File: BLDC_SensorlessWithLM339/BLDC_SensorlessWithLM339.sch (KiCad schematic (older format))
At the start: 48 parts, among them J1 Conn_01x04_Female, J2 Conn_01x07_Female, J3 Screw_Terminal_01x02, J4 Screw_Terminal_01x03, Q1 50N06, Q2 50N06, Q3 50N06, Q4 50N06, Q5 50N06, Q6 50N06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

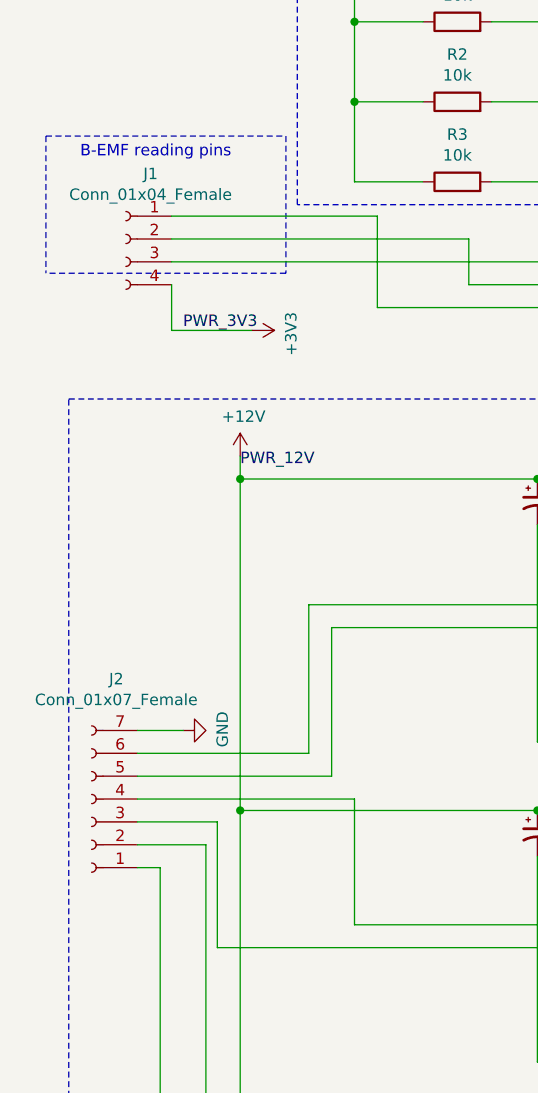
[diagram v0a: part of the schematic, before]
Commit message: Updated to Version 0.2
Updated to version 0.2. Now pcb holds only 10x10 cm^2 field.
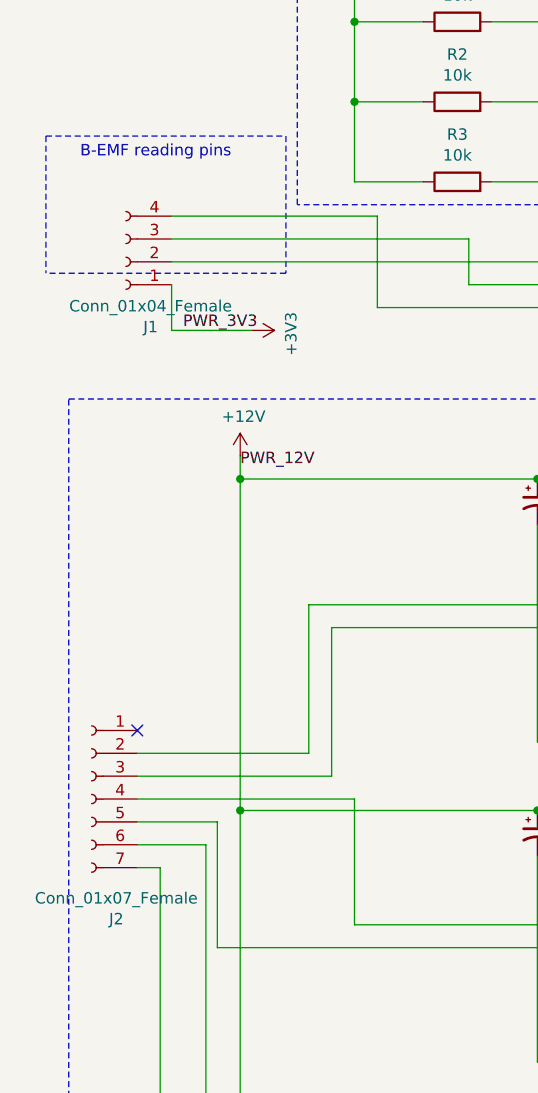
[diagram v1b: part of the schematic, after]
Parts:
- J1: footprint Connector_PinSocket_1.27mm:PinSocket_1x04_P1.27mm_Vertical -> Connector_PinSocket_2.54mm:PinSocket_1x04_P2.54mm_Vertical
- J2: footprint Connector_PinSocket_1.27mm:PinSocket_1x07_P1.27mm_Vertical -> Connector_PinSocket_2.54mm:PinSocket_1x07_P2.54mm_Vertical
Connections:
- net +3V3: now also J1.1 (Pin_1); no longer J1.4 (Pin_4)
- net GND: no longer J2.7 (Pin_7)
- net at R2.2, U4.1 (OUT2): now also J1.3 (Pin_3); no longer J1.2 (Pin_2)
- net at R1.2, U4.14 (OUT3): now also J1.2 (Pin_2); no longer J1.3 (Pin_3)
- net at R3.2, U4.2 (OUT1): now also J1.4 (Pin_4); no longer J1.1 (Pin_1)
- net at J2.1 (Pin_1): no longer U3.3 (LIN)
- net at J2.2 (Pin_2): now also U1.2 (HIN); no longer U3.2 (HIN)
- net at J2.3 (Pin_3): now also U1.3 (LIN); no longer U2.3 (LIN)
- net at J2.5 (Pin_5): now also U2.3 (LIN); no longer U1.3 (LIN)
- net at J2.6 (Pin_6): now also U3.2 (HIN); no longer U1.2 (HIN)
- new net: J2.7 (Pin_7), U3.3 (LIN)
- no-connect marks 0 -> 1
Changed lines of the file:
@@
 Sheet 1 1
 Title "Sensorless BLDC Electronic Speed Controller "
-Date "2020-12-10"
+Date "2020-12-14"
 Rev "0.1"
 Comp "Ahmet Kaan Büyükkaya"
@@
 Wire Notes Line
 	6250 7750 600  7750
-Wire Notes Line
-	600  7750 600  2850
 Wire Notes Line
 	6600 700  6600 3750
@@
 PWR_12V
 $Comp
-L Connector:Conn_01x04_Female J1
-U 1 1 5FE1C085
-P 850 2150
-F 0 "J1" H 742 2435 50  0000 C CNN
-F 1 "Conn_01x04_Female" H 742 2344 50  0000 C CNN
-F 2 "Connector_PinSocket_1.27mm:PinSocket_1x04_P1.27mm_Vertical" H 850 2150 50  0001 C CNN
-F 3 "~" H 850 2150 50  0001 C CNN
-	1    850  2150
-	-1   0    0    -1
-$EndComp
-$Comp
 L power:+3V3 #PWR03
 U 1 1 5FE2AD01
@@
 PWR_3V3
 $Comp
-L power:GND #PWR01
-U 1 1 5FD00A0A
-P 1100 4300
-F 0 "#PWR01" H 1100 4050 50  0001 C CNN
-F 1 "GND" H 1105 4127 50  0000 C CNN
-F 2 "" H 1100 4300 50  0001 C CNN
-F 3 "" H 1100 4300 50  0001 C CNN
-	1    1100 4300
-	0    -1   -1   0
-$EndComp
-Wire Wire Line
-	900  4300 1100 4300
-$Comp
 L Connector:Screw_Terminal_01x02 J3
 U 1 1 5FD10C4B
@@
 Wire Wire Line
 	900  4800 1200 4800
-$Comp
-L Connector:Conn_01x07_Female J2
-U 1 1 5FCF1D83
-P 700 4600
-F 0 "J2" H 592 4075 50  0000 C CNN
-F 1 "Conn_01x07_Female" H 592 4166 50  0000 C CNN
-F 2 "Connector_PinSocket_1.27mm:PinSocket_1x07_P1.27mm_Vertical" H 700 4600 50  0001 C CNN
-F 3 "~" H 700 4600 50  0001 C CNN
-	1    700  4600
-	-1   0    0    1
-$EndComp
 $Comp
 L power:GND #PWR?
@@
 Wire Notes Line
 	500  1700 1550 1700
-Wire Notes Line
-	1550 2300 500  2300
 Text Notes 650  1800 0    50   ~ 0
 B-EMF reading pins
@@
 Wire Notes Line
 	500  1700 500  2300
+Wire Notes Line
+	1550 2300 500  2300
+NoConn ~ 900  4300
+$Comp
+L Connector:Conn_01x04_Female J1
+U 1 1 5FE1C085
+P 850 2250
+F 0 "J1" H 742 2535 50  0000 C CNN
+F 1 "Conn_01x04_Female" H 742 2444 50  0000 C CNN
+F 2 "Connector_PinSocket_2.54mm:PinSocket_1x04_P2.54mm_Vertical" H 850 2250 50  0001 C CNN
+F 3 "~" H 850 2250 50  0001 C CNN
+	1    850  2250
+	-1   0    0    1
+$EndComp
+Wire Notes Line
+	600  7750 600  2850
+$Comp
+L Connector:Conn_01x07_Female J2
+U 1 1 5FCF1D83
+P 700 4600
+F 0 "J2" H 592 4075 50  0000 C CNN
+F 1 "Conn_01x07_Female" H 592 4166 50  0000 C CNN
+F 2 "Connector_PinSocket_2.54mm:PinSocket_1x07_P2.54mm_Vertical" H 700 4600 50  0001 C CNN
+F 3 "~" H 700 4600 50  0001 C CNN
+	1    700  4600
+	-1   0    0    -1
+$EndComp
 $EndSCHEMATC
